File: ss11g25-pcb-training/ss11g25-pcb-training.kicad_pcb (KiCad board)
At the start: 2 copper layers, 11 parts, among them U2 LMR33630CDDA

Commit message: Newest updates
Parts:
- moved Cin1 34.3 mm to (92.2, 55.5), turned to 90 degrees
- moved U2 32.8 mm to (100.4, 53.4)
- moved Chf1 31.0 mm to (94.5, 55.5), turned to 90 degrees
- moved Rfbb1 30.1 mm to (97.5, 61.5)
- moved R1 27.0 mm to (100.5, 60.0)
- moved Rfbt1 25.1 mm to (113.0, 55.3), turned to 90 degrees
- moved L1 24.7 mm to (107.2, 52.3)
- moved Cout1 23.0 mm to (115.0, 55.3), turned to -90 degrees
- moved Cvcc1 20.3 mm to (107.2, 56.8)
- moved Cbt1 18.9 mm to (106.9, 54.3)
- moved Cff1 17.4 mm to (111.2, 55.3), turned to -90 degrees
- renumbered Cboot1 to Cbt1
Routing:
- net GNDREF: track 0.00 -> 46.0 mm
- net Net-(U2-FB): track 0.00 -> 21.4 mm
- net Net-(U2-VCC): track 0.00 -> 9.38 mm
- net VDD (5V 3A): track 0.00 -> 8.11 mm
- net VDD (6V -> 36V): track 0.00 -> 6.86 mm
- net Net-(U2-SW): track 0.00 -> 5.41 mm
- net Net-(U2-BOOT): track 0.00 -> 5.10 mm
- net VDD (PG): track 0.00 -> 2.60 mm
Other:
- board outline added: 26.7 x 12.7 mm

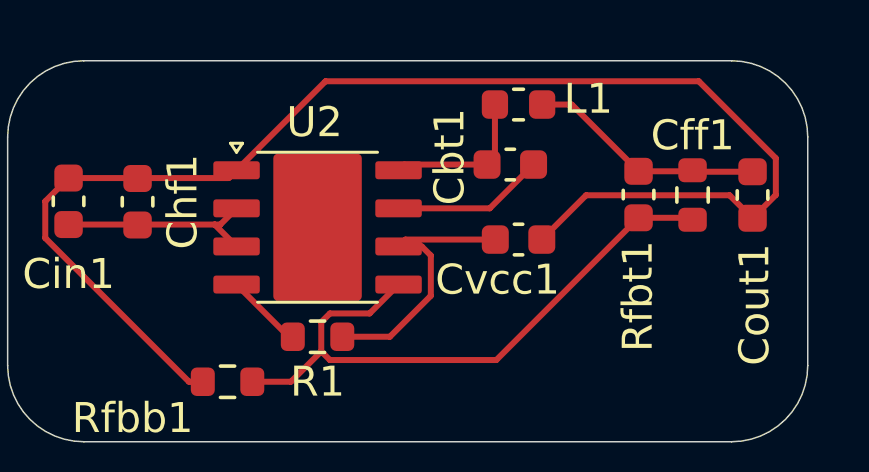
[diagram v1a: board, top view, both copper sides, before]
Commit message: Footpint Fix
TP Pad fix, so DRC doesn't get mad.
One error - relating to local save of footprint alter
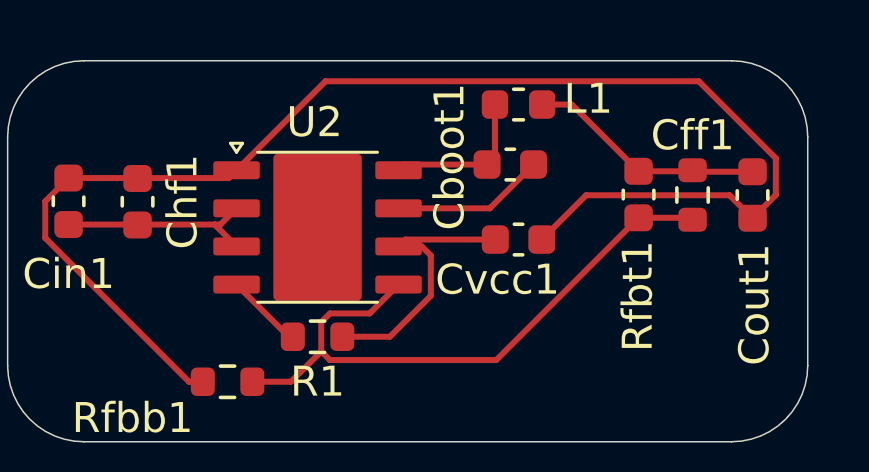
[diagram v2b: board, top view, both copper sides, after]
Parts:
- renumbered Cbt1 to Cboot1
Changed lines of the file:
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@@
 		(descr "Capacitor SMD 0603 (1608 Metric), square (rectangular) end terminal, IPC-7351 nominal, (Body size source: IPC-SM-782 page 76, https://www.pcb-3d.com/wordpress/wp-content/uploads/ipc-sm-782a_amendment_1_and_2.pdf), generated with kicad-footprint-generator")
 		(tags "capacitor")
-		(property "Reference" "Cbt1"
+		(property "Reference" "Cboot1"
 			(at -2.025 -0.26 90)
 			(layer "F.SilkS")
@@
 			)
 		)
-		(property "Datasheet" "https://www.ti.com/lit/ds/symlink/lmr33630.pdf?ts=1758180545971&ref_url=https%253A%252F%252Fwww.ti.com%252Fproduct%252FLMR33630%252Fpart-details%252FLMR33630ADDAR%253Futm_source%253Dgoogle%2526utm_medium%253Dcpc%2526utm_campaign%253Dapp-null-null-app_opn_en-cpc-storeic-google-eu_en_pur%2526utm_content%253DDevice%2526ds_k%253DLMR33630ADDAR%2526DCM%253Dyes%2526gclsrc%253Daw.ds%2526gad_source%253D1%2526gad_campaignid%253D18945642618%2526gbraid%253D0AAAAAC068F1yPR6eGT_H3Bx1R9sMnZ6vk%2526gclid%253DCj0KCQjw267GBhCSARIsAOjVJ4HOCgV3wTCcxJkMu-GTEI24lwOIhRNu7yLXUiGQngPs8SUHWE71Q0kaAluFEALw_wcB"
+		(property "Datasheet" ""
 			(at 0 0 0)
 			(unlocked yes)
@@
 			)
 		)
-		(pad "" smd roundrect
-			(at 0.1 3)
-			(size 2.71 3.4)
-			(layers "F.Cu" "F.Mask" "F.Paste")
-			(roundrect_rratio 0.05)
-		)
 		(pad "1" smd roundrect
 			(at -2.6 1.1)
@@
 		)
 		(pad "TP" smd roundrect
+			(at 0.1 3)
+			(size 2.71 3.4)
+			(layers "F.Cu" "F.Mask" "F.Paste")
+			(roundrect_rratio 0.05)
+			(net 5 "GNDREF")
+			(pinfunction "AGND")
+			(pintype "power_in")
+		)
+		(pad "TP" smd roundrect
